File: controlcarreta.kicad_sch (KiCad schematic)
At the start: 39 parts, among them J1 Screw_Terminal_01x02, J1255 Conn_Coaxial, J18 FTDI_AUTOPROG, J2 Screw_Terminal_01x02, J20 SMA GNSS, J3 Conn_01x04_Male, Q1 SI4447ADY-T1-GE3, Q2 SS8050, Q3 SS8050, SW1 RESET, SW2 BOOT, U1 ESP32-S3-WROOM-1-N8

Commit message: friday changes
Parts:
- C14: DigiKey (none) -> 490-1691-2-ND; MPN (none) -> GRM21BR71C105KA01L; Manufacturer (none) -> Murata Electronics
- C15: DigiKey (none) -> 1276-1003-2-ND; MPN (none) -> CL21B104KBCNNNC; Manufacturer (none) -> Samsung Electro-Mechanics
- C5, C9: DigiKey (none) -> 490-14466-2-ND; MPN (none) -> GRM21BR71C475KE51L; Manufacturer (none) -> Murata Electronics
- D2, D3: DigiKey (none) -> 1655-1N4007FLTR-ND; MPN (none) -> 1N4007FL; Manufacturer (none) -> SMC Diode Solutions
- D4, D5: DigiKey (none) -> 732-5016-ND; MPN (none) -> 151051RS11000; Manufacturer (none) -> Würth Elektronik
- F1: DigiKey (none) -> 5923-0679L5000-05TR-ND; MPN (none) -> 0679L5000-05; Manufacturer (none) -> Bel Fuse Inc.
- J1, J2: DigiKey (none) -> ED2843-ND; MPN (none) -> OSTOQ025450; Manufacturer (none) -> On Shore Technology Inc.
- J1255: DigiKey (none) -> ARFX1231-ND; MPN (none) -> 901-144-8RFX; Manufacturer (none) -> Amphenol RF
- J18: DigiKey (none) -> 2223-SSK01-MPH-254-A6-ND; MPN (none) -> SSK01-MPH-254-A6; Manufacturer (none) -> Same Sky (Formerly CUI Devices)
- J20: DigiKey (none) -> ARFX1231-ND
- J3: DigiKey (none) -> 2223-SSK01-MPH-254-A4-ND; MPN (none) -> SSK01-MPH-254-A4; Manufacturer (none) -> Same Sky (Formerly CUI Devices)
- Q1: DigiKey (none) -> SI4447ADY-T1-GE3TR-ND; MPN (none) -> SI4447ADY-T1-GE3; Manufacturer (none) -> Vishay Siliconix
- Q2, Q3: DigiKey (none) -> 641-1790-2-ND; MPN (none) -> SS8050-G; Manufacturer (none) -> Comchip Technology
- R10: DigiKey (none) -> 311-100KFRTR-ND; MPN (none) -> RC1206FR-07100KL; Manufacturer (none) -> YAGEO
- R100, R13, R14, R3, R4: DigiKey (none) -> RMCF1206FT10K0TR-ND; MPN (none) -> RMCF1206FT10K0; Manufacturer (none) -> Stackpole Electronics Inc
- R11: DigiKey (none) -> 118-CR1206-JW-223ELFTR-ND; MPN (none) -> CR1206-JW-223ELF; Manufacturer (none) -> Bourns Inc.
- R12: DigiKey (none) -> 311-1.00KFRTR-ND; MPN (none) -> RC1206FR-071KL; Manufacturer (none) -> YAGEO
- R30, R31: DigiKey (none) -> RMCF1206FT12K0TR-ND; MPN (none) -> RMCF1206FT12K0; Manufacturer (none) -> Stackpole Electronics Inc
- R5: DigiKey (none) -> 738-RNCF1206TKY1K50TR-ND; MPN (none) -> RNCF1206TKY1K50; Manufacturer (none) -> Stackpole Electronics Inc
- R8, R9: DigiKey (none) -> 311-330ERTR-ND; MPN (none) -> RC1206JR-07330RL; Manufacturer (none) -> YAGEO
- SW1, SW2: DigiKey (none) -> SW400-ND
- U1: DigiKey (none) -> 5407-ESP32-S3-WROOM-1-N8TR-ND

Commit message: schematic updated
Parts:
- removed C5, C9: 4.7 uF, Capacitor_SMD:C_0805_2012Metric_Pad1.18x1.45mm_HandSolder, symbol pspice:C
- removed D2, D3: 1N4007, Diode_SMD:D_SOD-123F, symbol Diode:1N4007
- removed J1255: Conn_Coaxial, Connector_Coaxial:SMA_Amphenol_132134-16_Vertical, symbol Connector:Conn_Coaxial
- removed J20: SMA GNSS, Connector_Coaxial:SMA_Amphenol_132134-16_Vertical, symbol Connector:Conn_Coaxial
- removed J3: Conn_01x04_Male, Connector_PinHeader_2.54mm:PinHeader_1x04_P2.54mm_Vertical, symbol Connector:Conn_01x04_Male
- removed R3: 10k, Resistor_SMD:R_1206_3216Metric_Pad1.30x1.75mm_HandSolder, symbol Device:R
- removed R5: 1.5k, Resistor_SMD:R_1206_3216Metric_Pad1.30x1.75mm_HandSolder, symbol Device:R
- F1: value 0679L5000-05 -> 2A; DigiKey 5923-0679L5000-05TR-ND -> 5923-0680L2000-05TR-ND; MPN 0679L5000-05 -> 0680L2000-05; PARTREV 0679H Apr2019 -> 0680L Jan2026
- renumbered C14 to C1, C15 to C2, D6 to D1, D4 to D2, D5 to D3, J18 to J3, R10 to R1, R8 to R10, R9 to R11, R13 to R2, R14 to R3, R11 to R4, R12 to R5, R4 to R6, R30 to R7, R31 to R8, R100 to R9
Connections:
- net RX_GPS: no longer names the net of U1.5 (IO5)
- net TX_GPS: no longer names the net of U1.4 (IO4)
- no-connect marks 2 -> 4
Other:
- moved on the sheet: D1, D2, D3, F1, J1, J2, Q1, R1, R10, R11, R4, R5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

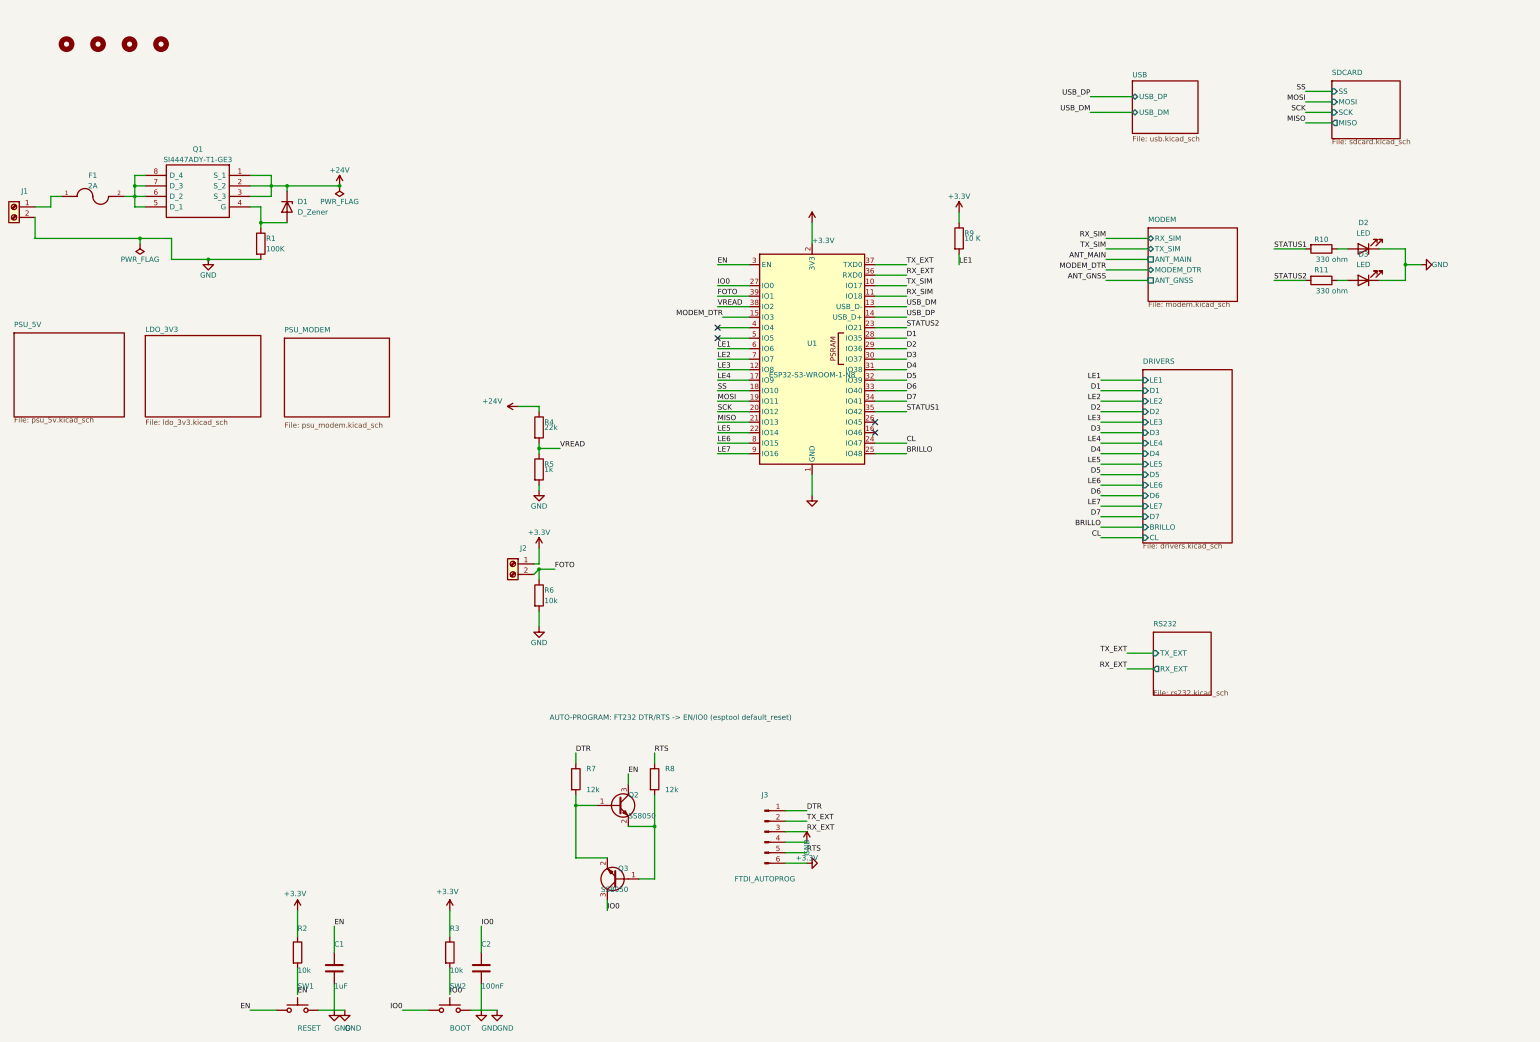
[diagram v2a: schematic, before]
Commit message: removed gps headear
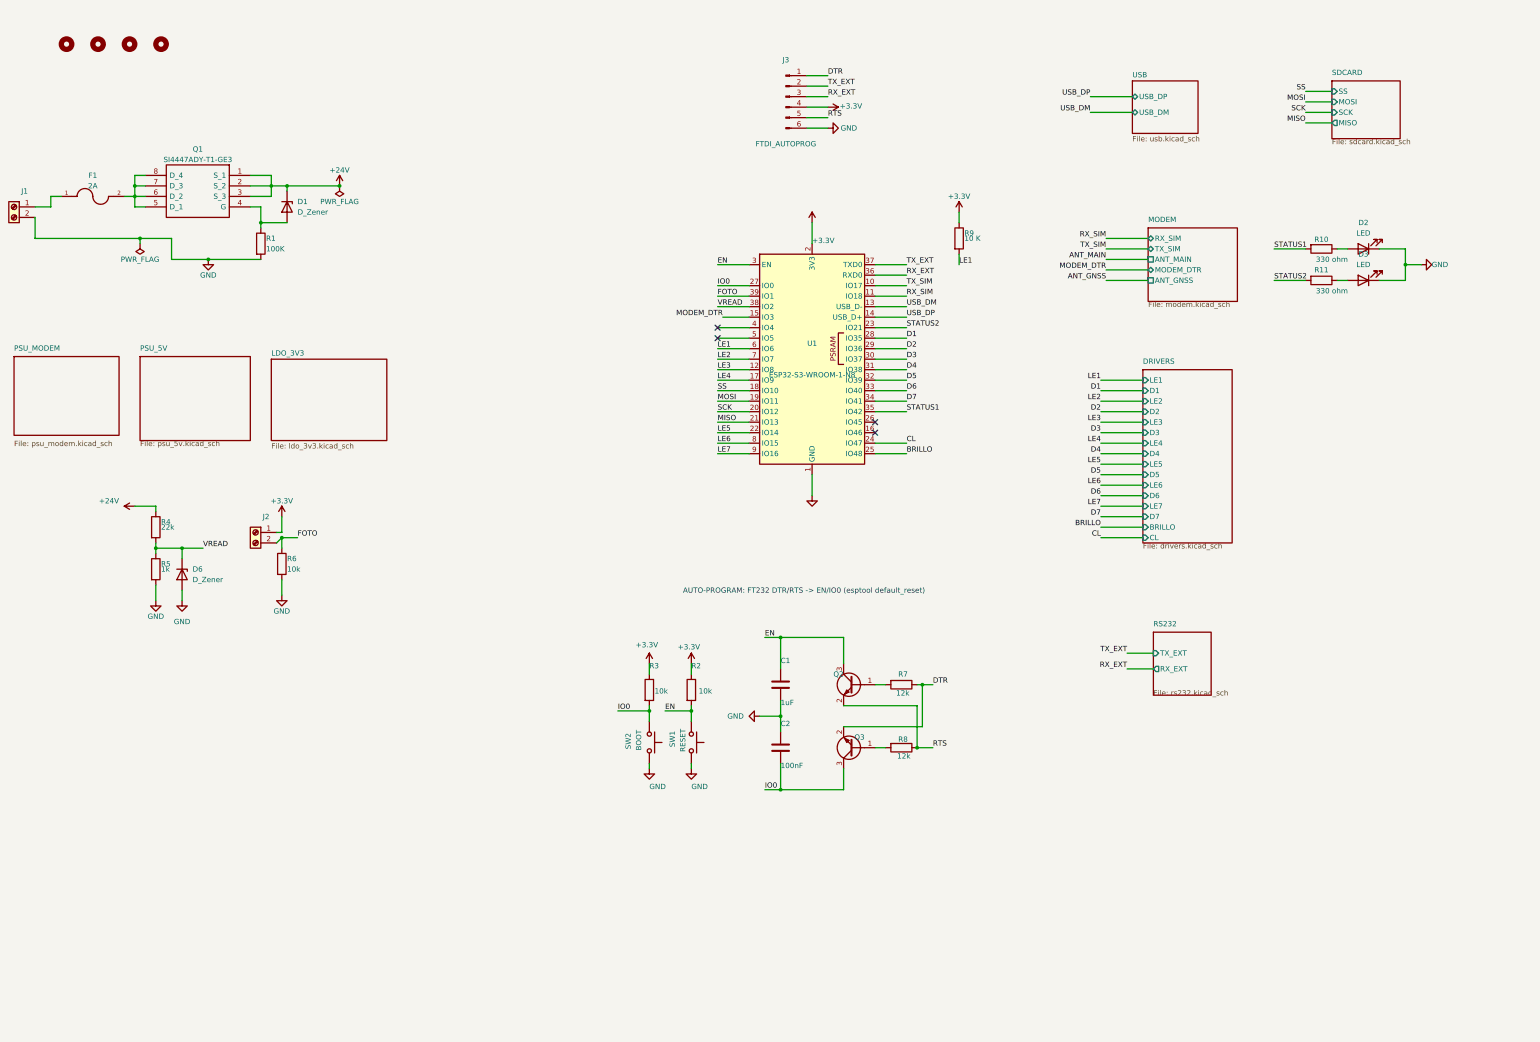
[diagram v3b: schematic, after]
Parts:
- added D6: D_Zener, Diode_SMD:D_SOD-123, symbol Device:D_Zener
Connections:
- net DTR: now also Q3.2 (E)
- net GND: now also C2.1, D6.2 (A); no longer C2.2
- net IO0: now also C2.2; no longer C2.1
- net RTS: now also Q2.2 (E)
- net VREAD: now also D6.1 (K)
- net at Q3.1 (B), R8.2: no longer Q2.2 (E)
- net at Q2.1 (B), R7.2: no longer Q3.2 (E)
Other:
- moved on the sheet: C1, C2, J2, J3, Q2, Q3, R2, R3, R4, R5, R6, R7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

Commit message: prettier schematic
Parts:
- removed H1, H2, H3, H4: MountingHole, MountingHole:MountingHole_4.3mm_M4, symbol Mechanical:MountingHole
- D1: DigiKey (none) -> MMSZ15T1GOSCT-ND; MPN (none) -> MMSZ15T1G; Manufacturer (none) -> onsemi
- D6: DigiKey (none) -> MMSZ3V3T1GOSCT-ND; MPN (none) -> MMSZ3V3T1G; Manufacturer (none) -> onsemi
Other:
- added sheet Mechanical (mechanical.kicad_sch)
- moved on the sheet: C1, C2, D1, D2, D3, D6, F1, J1, J2, J3, Q1, Q2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

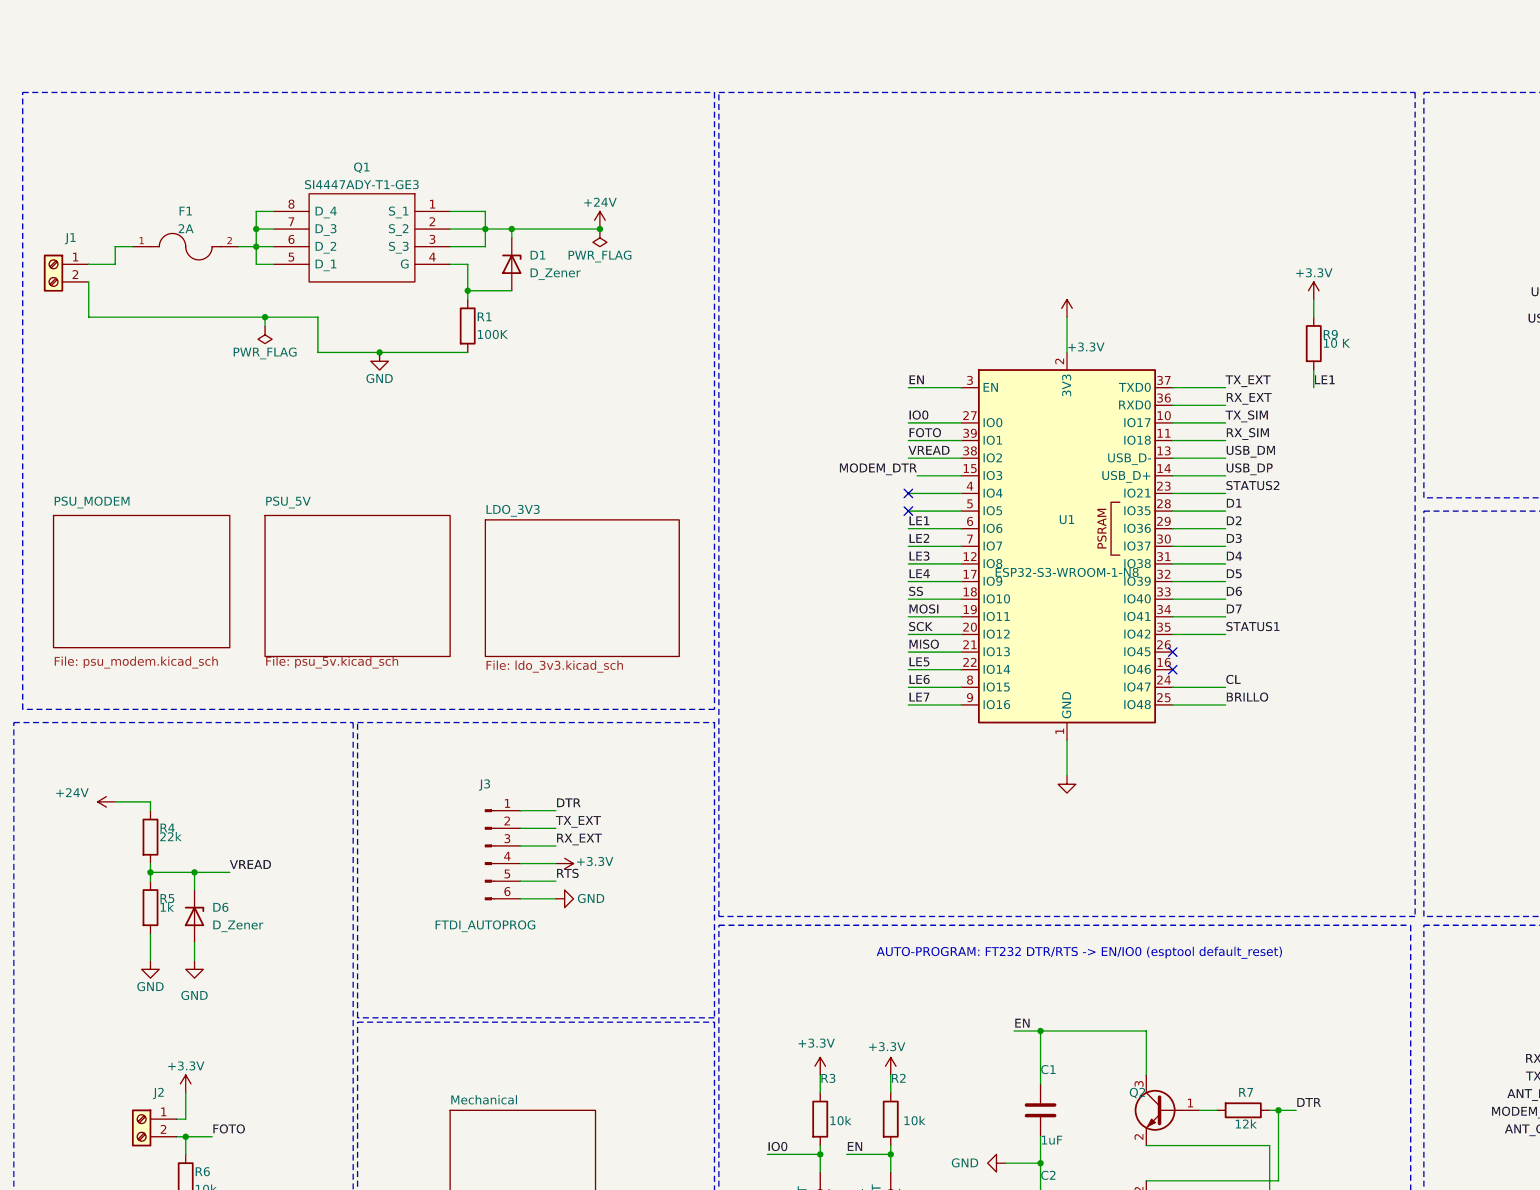
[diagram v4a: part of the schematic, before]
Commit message: 2 power source
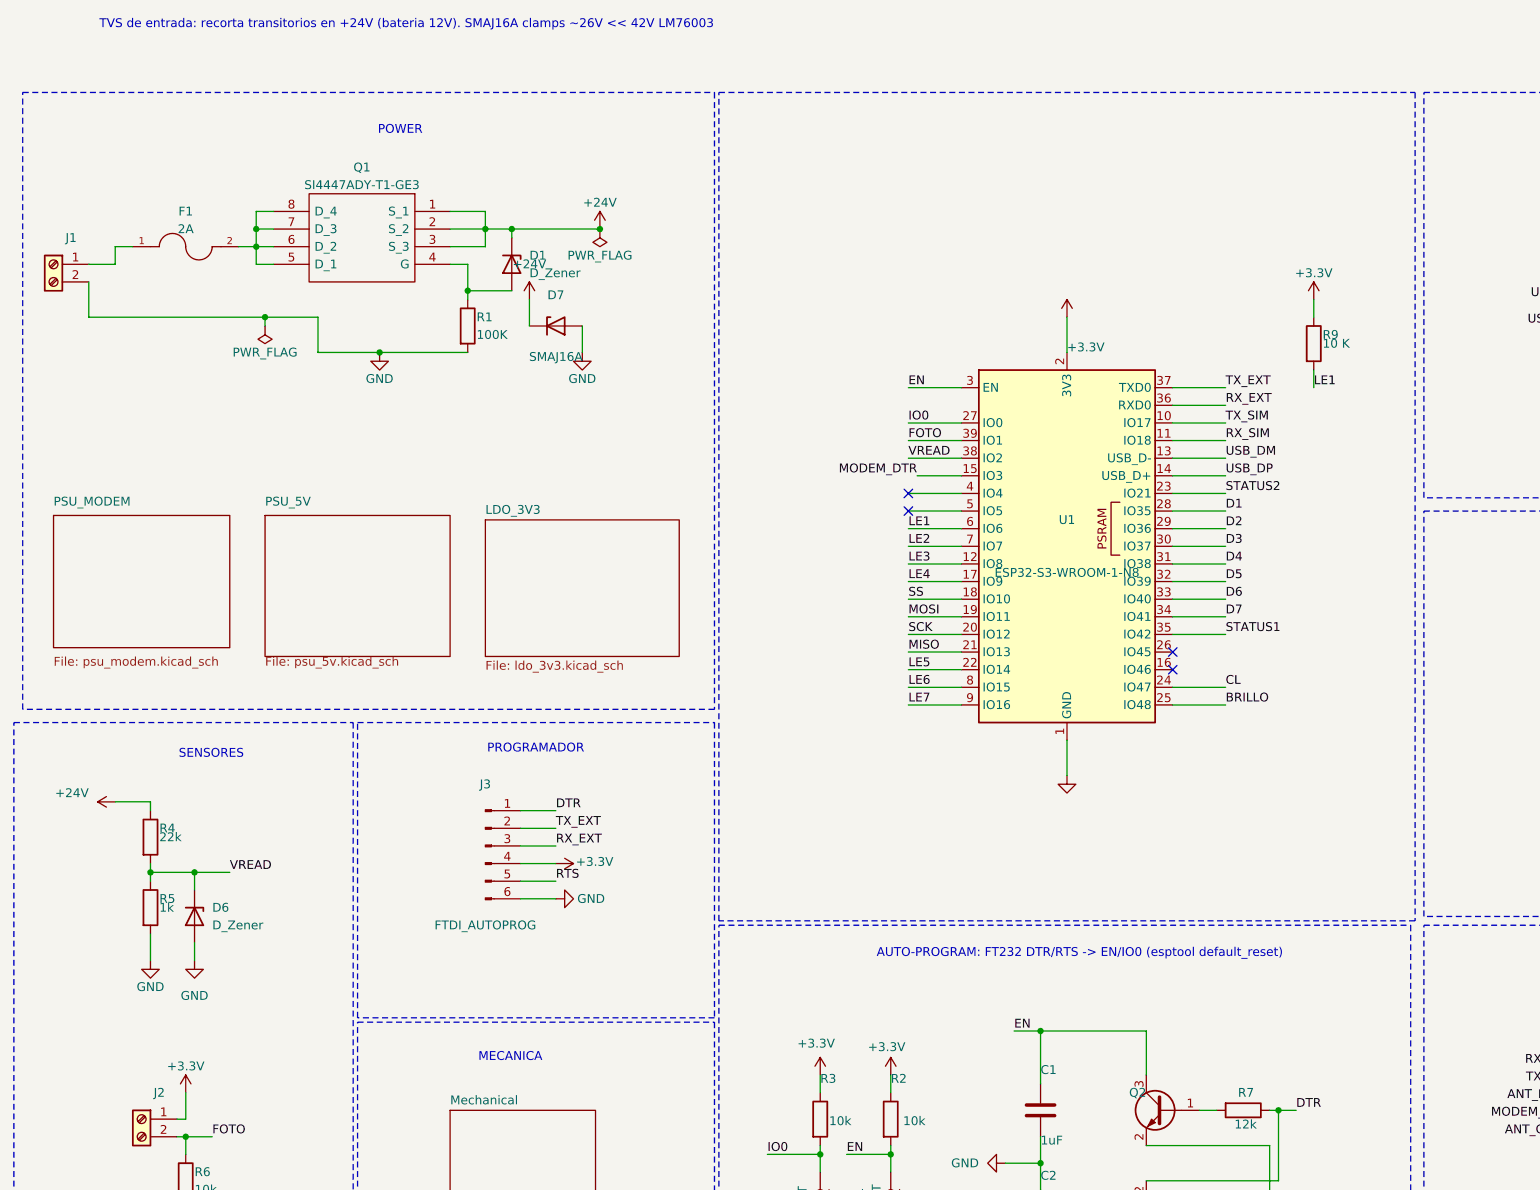
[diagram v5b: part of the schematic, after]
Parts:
- added D7: SMAJ16A, Diode_SMD:D_SMA, symbol Device:D_Zener
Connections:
- net +24V: now also D7.1 (K)
- net GND: now also D7.2 (A)
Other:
- note added: "MECANICA"
- note added: "POWER"
- note added: "PROGRAMADOR"
- note added: "SENSORES"
- note added: "TVS de entrada: recorta transitorios en +24V (bateria 12V). SMAJ16A clamps ~26V << 42V LM76003"

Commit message: last changes in work
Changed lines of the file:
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@@
 	)
 	(label "EN"
-		(at 163.83 97.79 0)
+		(at 163.83 97.79 180)
 		(effects
 			(font
 				(size 1.27 1.27)
 			)
-			(justify left bottom)
+			(justify right bottom)
 		)
 	)
 	(label "IO0"
-		(at 163.83 102.87 0)
+		(at 163.83 102.87 180)
 		(effects
 			(font
 				(size 1.27 1.27)
 			)
-			(justify left bottom)
+			(justify right bottom)
 		)
 	)
 	(label "FOTO"
-		(at 163.83 105.41 0)
+		(at 163.83 105.41 180)
 		(effects
 			(font
 				(size 1.27 1.27)
 			)
-			(justify left bottom)
+			(justify right bottom)
 		)
 	)
 	(label "VREAD"
-		(at 163.83 107.95 0)
+		(at 163.83 107.95 180)
 		(effects
 			(font
 				(size 1.27 1.27)
 			)
-			(justify left bottom)
+			(justify right bottom)
 		)
 	)
 	(label "LE1"
-		(at 163.83 118.11 0)
+		(at 163.83 118.11 180)
 		(effects
 			(font
 				(size 1.27 1.27)
 			)
-			(justify left bottom)
+			(justify right bottom)
 		)
 	)
 	(label "LE2"
-		(at 163.83 120.65 0)
+		(at 163.83 120.65 180)
 		(effects
 			(font
 				(size 1.27 1.27)
 			)
-			(justify left bottom)
+			(justify right bottom)
 		)
 	)
 	(label "LE3"
-		(at 163.83 123.19 0)
+		(at 163.83 123.19 180)
 		(effects
 			(font
 				(size 1.27 1.27)
 			)
-			(justify left bottom)
+			(justify right bottom)
 		)
 	)
 	(label "LE4"
-		(at 163.83 125.73 0)
+		(at 163.83 125.73 180)
 		(effects
 			(font
 				(size 1.27 1.27)
 			)
-			(justify left bottom)
+			(justify right bottom)
 		)
 	)
 	(label "SS"
-		(at 163.83 128.27 0)
+		(at 163.83 128.27 180)
 		(effects
 			(font
 				(size 1.27 1.27)
 			)
-			(justify left bottom)
+			(justify right bottom)
 		)
 	)
 	(label "MOSI"
-		(at 163.83 130.81 0)
+		(at 163.83 130.81 180)
 		(effects
 			(font
 				(size 1.27 1.27)
 			)
-			(justify left bottom)
+			(justify right bottom)
 		)
 	)
 	(label "SCK"
-		(at 163.83 133.35 0)
+		(at 163.83 133.35 180)
 		(effects
 			(font
 				(size 1.27 1.27)
 			)
-			(justify left bottom)
+			(justify right bottom)
 		)
 	)
 	(label "MISO"
-		(at 163.83 135.89 0)
+		(at 163.83 135.89 180)
 		(effects
 			(font
 				(size 1.27 1.27)
 			)
-			(justify left bottom)
+			(justify right bottom)
 		)
 	)
 	(label "LE5"
-		(at 163.83 138.43 0)
+		(at 163.83 138.43 180)
 		(effects
 			(font
 				(size 1.27 1.27)
 			)
-			(justify left bottom)
+			(justify right bottom)
 		)
 	)
 	(label "LE6"
-		(at 163.83 140.97 0)
+		(at 163.83 140.97 180)
 		(effects
 			(font
 				(size 1.27 1.27)
 			)
-			(justify left bottom)
+			(justify right bottom)
 		)
 	)
 	(label "LE7"
-		(at 163.83 143.51 0)
+		(at 163.83 143.51 180)
 		(effects
 			(font
 				(size 1.27 1.27)
 			)
-			(justify left bottom)
+			(justify right bottom)
 		)
 	)
@@
 		(dnp no)
 		(property "Reference" "R5"
-			(at 55.88 171.45 0)
+			(at 50.038 172.72 0)
 			(effects
 				(font
@@
 		(dnp no)
 		(property "Reference" "R4"
-			(at 55.88 161.29 0)
+			(at 50.038 162.56 0)
 			(effects
 				(font
@@
 		)
 		(property "Value" "ESP32-S3-WROOM-1-N8"
-			(at 186.69 124.46 0)
+			(at 186.69 161.544 0)
 			(effects
 				(font
@@
 		(dnp no)
 		(property "Reference" "R2"
-			(at 161.29 198.12 0)
+			(at 161.29 198.374 0)
 			(effects
 				(font
@@
 		(on_board yes)
 		(dnp no)
-		(fields_autoplaced yes)
 		(stroke
 			(width 0.1524)
@@
 		)
 		(property "Sheetfile" "rs232.kicad_sch"
-			(at 341.63 204.47 0)
+			(at 338.836 208.788 0)
 			(effects
 				(font
